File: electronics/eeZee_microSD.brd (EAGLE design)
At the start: 20.3 x 31.2 mm, 15 parts, among them U1 MCP1824S, U2 74HC4050

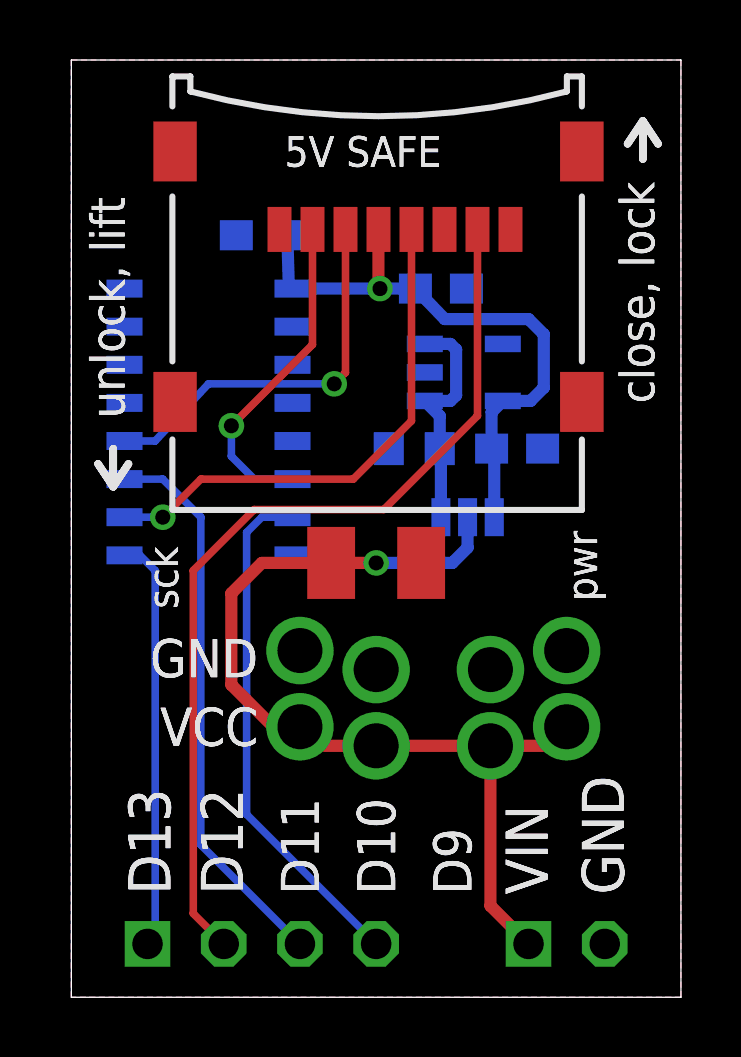
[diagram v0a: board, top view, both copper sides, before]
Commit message: Switched to push-pull socket, shrank board, modified regulator and level shifter layouts, modified silk layout.
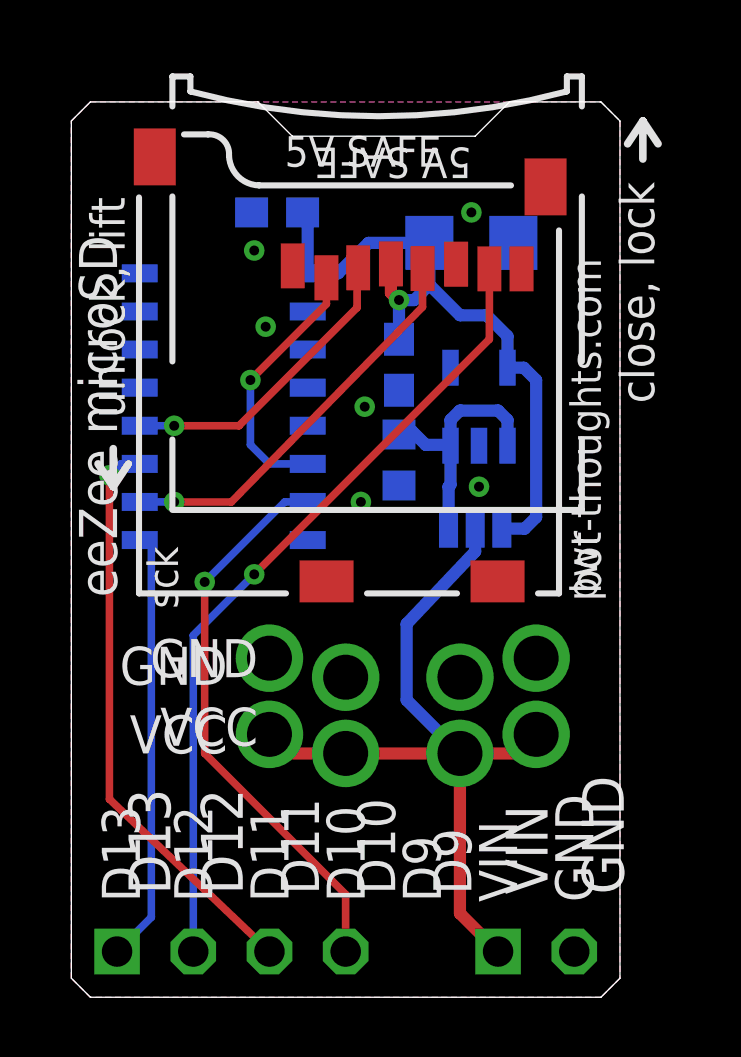
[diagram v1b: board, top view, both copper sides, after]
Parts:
- removed C4: 10uF, rcl:SMC_B
- removed U$1: MICROSD_TFLASH, mes_electromech:TFLASH_CP-0000-086
- added U3: USD-SOCKET, SparkFun-Connectors:MICROSD_1:1
- C1: value 1uF -> 106; device rcl:C0603 -> rcl:C1206
- C2, C3: value 0.1uF -> 104
- moved C3 4.83 mm to (10.9, 21.1), turned to 270 degrees
- moved C1 1.83 mm to (13.3, 25.1)
- moved U1 1.25 mm to (13.6, 19.7), turned to 0 degrees
- moved JP1 1.05 mm to (15.5, 1.52)
- moved JP2 1.05 mm to (15.5, 8.76)
- moved JP6 1.05 mm to (5.33, 1.52)
- moved JP3 1.05 mm to (9.14, 8.13)
- moved JP4 1.05 mm to (13.0, 8.13)
- moved JP5 1.05 mm to (6.60, 8.76)
- moved C2 0.92 mm to (6.86, 26.2)
- moved U2 0.72 mm to (5.08, 19.7)
- moved R5 0.63 mm to (10.9, 17.9), turned to 90 degrees
- moved REG 0.46 mm to (13.5, 15.6)
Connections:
- net !SS: now also U3.2; no longer U$1.CS
- net GND: now also U3.6, U3.CD1, U3.CD2, U3.GND1, U3.GND3; no longer C4.-, U$1.GND, U$1.SHIELD1, U$1.SHIELD2, U$1.SHIELD3, U$1.SHIELD4
- net MISO: now also U3.7; no longer U$1.DO
- net MOSI: now also U3.3; no longer U$1.DI
- net SCK: now also U3.5; no longer U$1.SCLK
- net VBOARD: no longer C4.+
- net VCC: now also U3.4; no longer U$1.VDD
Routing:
- net VBOARD: track 32.0 -> 25.7 mm, vias 1 -> 0
- net MISO: track 30.7 -> 26.8 mm, vias 0 -> 1
- net SCK: track 17.3 -> 13.4 mm
- net VCC: track 20.2 -> 23.4 mm
- net MOSI: track 13.1 -> 10.2 mm
- net !SS: track 11.0 -> 8.79 mm
- net !CS_HV: track 17.2 -> 18.8 mm, vias 0 -> 1
- net SCK_HV: track 13.8 -> 14.6 mm
- net VREGIN: track 7.87 -> 8.61 mm
- net MOSI_HV: track 18.7 -> 19.3 mm, vias 0 -> 1
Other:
- board size 20.3 x 31.2 mm -> 18.3 x 29.8 mm
- board text added: "CC-BY-SA"
- board text added: "R0.3A"
